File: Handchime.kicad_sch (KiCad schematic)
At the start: 24 parts, among them J1 USB_C_Receptacle_USB2.0_16P, J2 Pins, J3 SWD, SW0 BOOT, SW1 Row 0, Col 0, SW2 Row 0, Col 1, U1 STM32C071GBUx, U2 PRTR5V0U2X, U3 XC6206P332MR-G

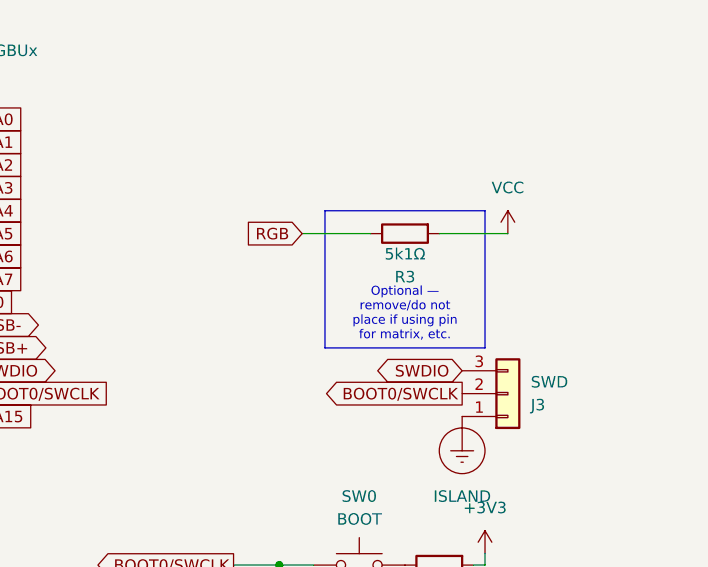
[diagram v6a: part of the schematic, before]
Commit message: Update labelling on optional RGB pull-op resistor
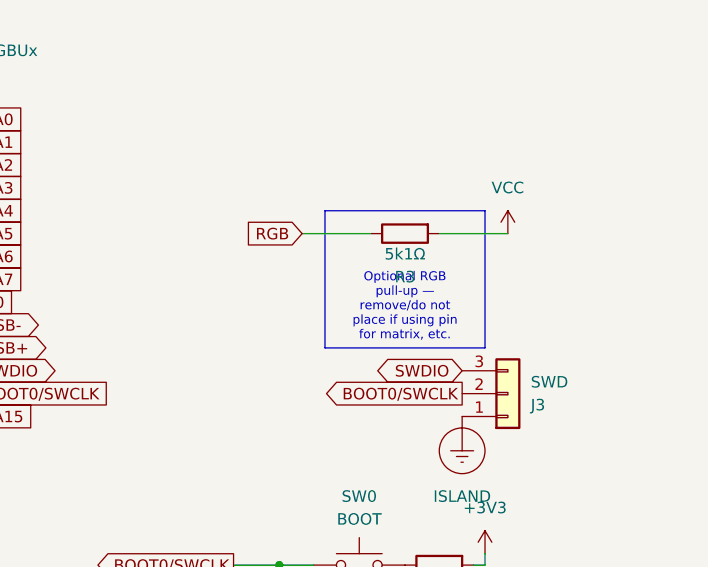
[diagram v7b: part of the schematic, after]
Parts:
- R3: Label (none) -> P
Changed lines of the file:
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@@
 		)
 	)
-	(text_box "Optional — remove/do not place if using pin for matrix, etc."
+	(text_box "Optional RGB pull-up — remove/do not place if using pin for matrix, etc."
 		(exclude_from_sim no)
 		(at 238.76 45.72 0)
@@
 			(at 247.65 48.26 90)
 			(hide yes)
+			(show_name no)
+			(do_not_autoplace no)
+			(effects
+				(font
+					(size 1.27 1.27)
+				)
+			)
+		)
+		(property "Label" "P"
+			(at 247.65 48.26 90)
+			(hide yes)

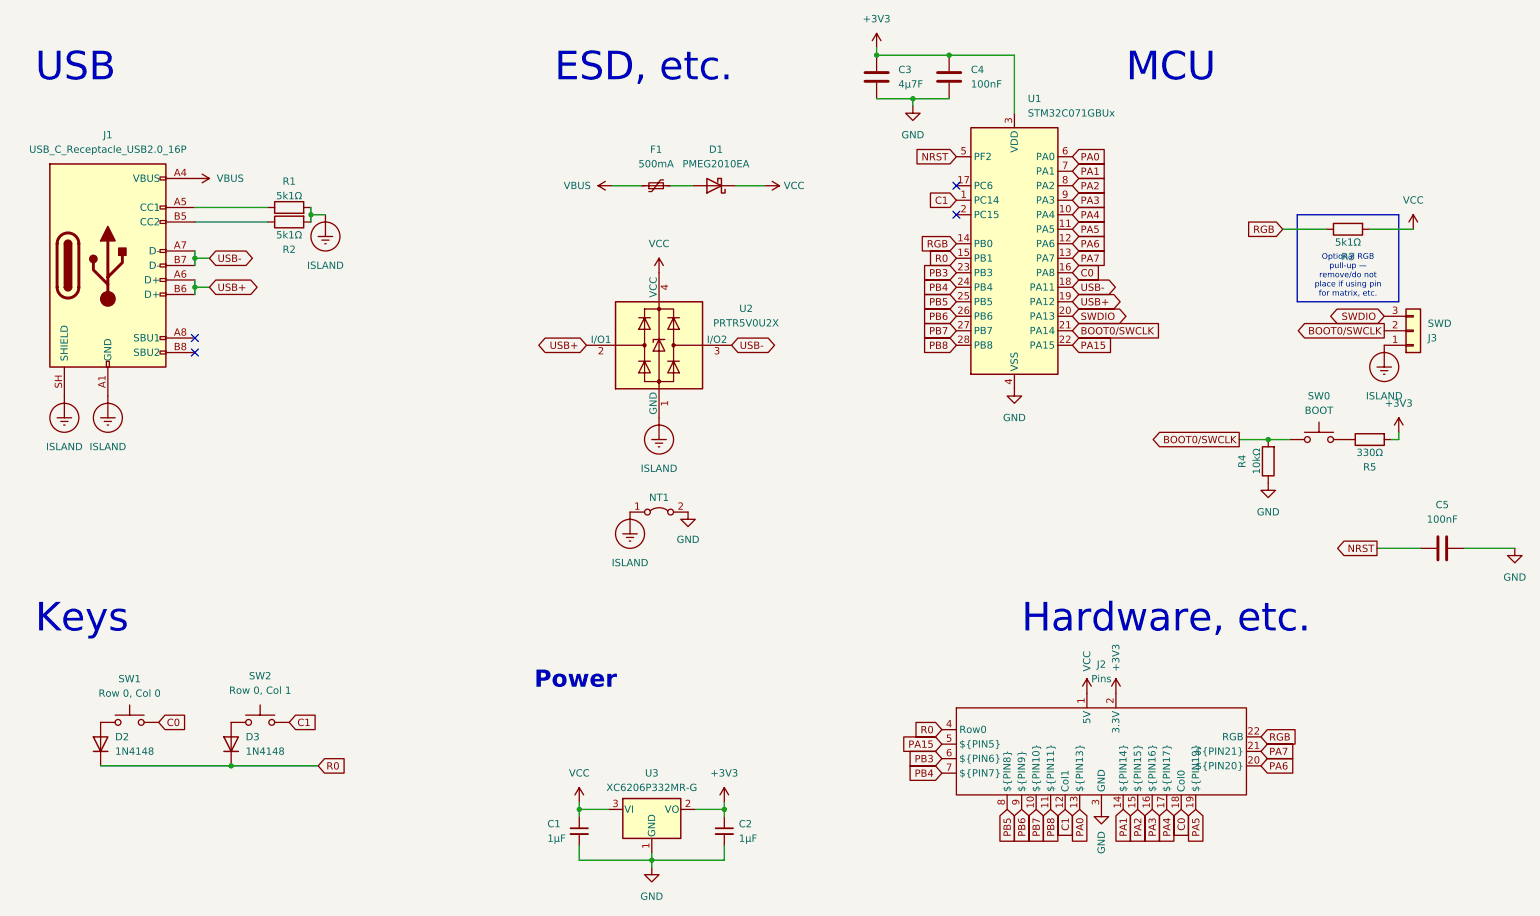
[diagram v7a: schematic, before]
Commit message: Add one extra GPIO pin access
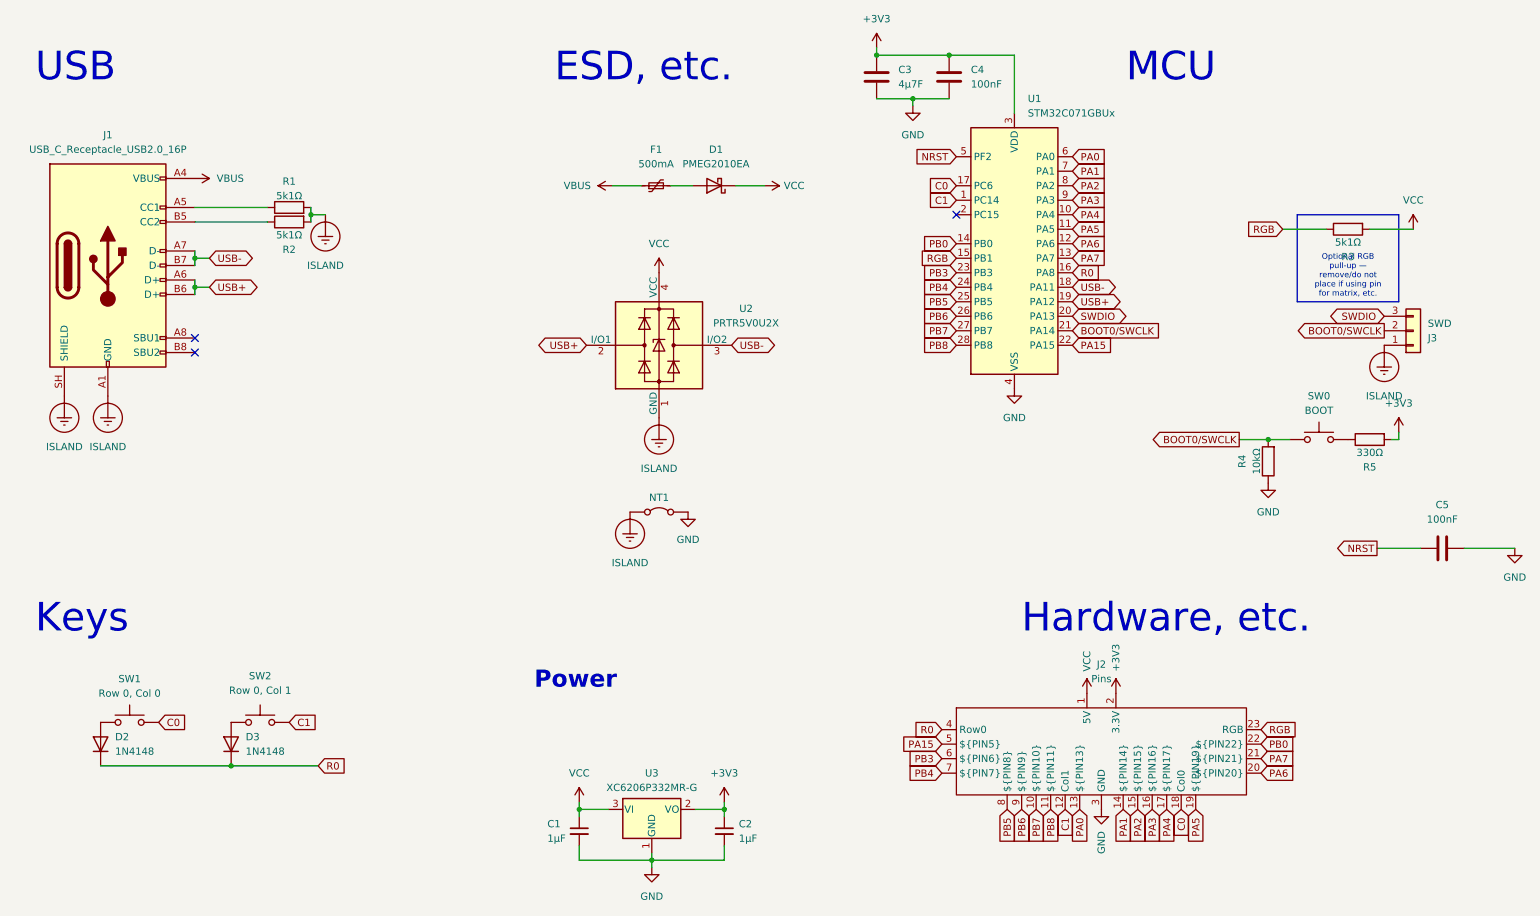
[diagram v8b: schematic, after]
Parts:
- J2: PIN22 (none) -> B0
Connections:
- net C0: now also U1.17 (PC6); no longer U1.16 (PA8)
- net R0: now also U1.16 (PA8); no longer U1.15 (PB1)
- net RGB: now also J2.23 (RGB), U1.15 (PB1); no longer J2.22 (RGB), U1.14 (PB0)
- new net PB0: J2.22 (${PIN22}), U1.14 (PB0)
- no-connect marks 4 -> 3
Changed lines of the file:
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@@
 	)
 	(no_connect
-		(at 179.07 40.64)
-	)
-	(no_connect
 		(at 45.72 67.31)
 	)
@@
 	(global_label "RGB"
 		(shape input)
-		(at 232.41 137.16 0)
+		(at 232.41 135.89 0)
 		(fields_autoplaced yes)
 		(effects
@@
 		)
 		(property "Intersheetrefs" "${INTERSHEET_REFS}"
-			(at 238.4645 137.16 0)
+			(at 238.4645 135.89 0)
 			(hide yes)
 			(show_name no)
@@
 		)
 	)
+	(global_label "PB0"
+		(shape input)
+		(at 232.41 138.43 0)
+		(fields_autoplaced yes)
+		(effects
+			(font
+				(size 1.27 1.27)
+			)
+			(justify left)
+		)
+		(property "Intersheetrefs" "${INTERSHEET_REFS}"
+			(at 238.3305 138.43 0)
+			(hide yes)
+			(show_name no)
+			(do_not_autoplace no)
+			(effects
+				(font
+					(size 1.27 1.27)
+				)
+				(justify left)
+			)
+		)
+	)
+	(global_label "C0"
+		(shape input)
+		(at 179.07 40.64 180)
+		(fields_autoplaced yes)
+		(effects
+			(font
+				(size 1.27 1.27)
+			)
+			(justify right)
+		)
+		(property "Intersheetrefs" "${INTERSHEET_REFS}"
+			(at 174.3146 40.64 0)
+			(hide yes)
+			(show_name no)
+			(do_not_autoplace no)
+			(effects
+				(font
+					(size 1.27 1.27)
+				)
+				(justify right)
+			)
+		)
+	)
 	(global_label "PA15"
 		(shape input)
@@
 	(global_label "PA6"
 		(shape input)
-		(at 232.41 142.24 0)
+		(at 232.41 143.51 0)
 		(fields_autoplaced yes)
 		(effects
@@
 		)
 		(property "Intersheetrefs" "${INTERSHEET_REFS}"
-			(at 238.0761 142.24 0)
+			(at 238.0761 143.51 0)
 			(hide yes)
 			(show_name no)
@@
 	(global_label "RGB"
 		(shape input)
-		(at 179.07 50.8 180)
+		(at 179.07 53.34 180)
 		(fields_autoplaced yes)
 		(effects
@@
 		)
 		(property "Intersheetrefs" "${INTERSHEET_REFS}"
-			(at 173.0155 50.8 0)
+			(at 173.0155 53.34 0)
 			(hide yes)
 			(show_name no)
@@
 	(global_label "PA7"
 		(shape input)
-		(at 232.41 139.7 0)
+		(at 232.41 140.97 0)
 		(fields_autoplaced yes)
 		(effects
@@
 		)
 		(property "Intersheetrefs" "${INTERSHEET_REFS}"
-			(at 237.9099 139.7 0)
+			(at 237.9099 140.97 0)
 			(hide yes)
 			(show_name no)
@@
 		)
 	)
-	(global_label "NRST"
-		(shape output)
-		(at 252.73 104.14 180)
+	(global_label "R0"
+		(shape input)
+		(at 199.39 55.88 0)
 		(fields_autoplaced yes)
 		(effects
@@
 				(size 1.27 1.27)
 			)
-			(justify right)
+			(justify left)
 		)
 		(property "Intersheetrefs" "${INTERSHEET_REFS}"
-			(at 245.7673 104.14 0)
+			(at 204.2571 55.88 0)
 			(hide yes)
 			(show_name no)
@@
 					(size 1.27 1.27)
 				)
-				(justify right)
+				(justify left)
 			)
 		)
 	)
-	(global_label "R0"
-		(shape input)
-		(at 179.07 53.34 180)
+	(global_label "NRST"
+		(shape output)
+		(at 252.73 104.14 180)
 		(fields_autoplaced yes)
 		(effects
@@
 		)
 		(property "Intersheetrefs" "${INTERSHEET_REFS}"
-			(at 174.2029 53.34 0)
+			(at 245.7673 104.14 0)
 			(hide yes)
 			(show_name no)
@@
 		)
 	)
-	(global_label "PB7"
+	(global_label "PB0"
 		(shape input)
-		(at 193.04 149.86 270)
+		(at 179.07 50.8 180)
 		(fields_autoplaced yes)
 		(effects
@@
 		)
 		(property "Intersheetrefs" "${INTERSHEET_REFS}"
-			(at 193.04 155.5733 90)
+			(at 173.1495 50.8 0)
 			(hide yes)
 			(show_name no)
@@
 		)
 	)
-	(global_label "C0"
+	(global_label "PB7"
 		(shape input)
-		(at 199.39 55.88 0)
+		(at 193.04 149.86 270)
 		(fields_autoplaced yes)
 		(effects
@@
 				(size 1.27 1.27)
 			)
-			(justify left)
+			(justify right)
 		)
 		(property "Intersheetrefs" "${INTERSHEET_REFS}"
-			(at 204.1454 55.88 0)
+			(at 193.04 155.5733 90)
 			(hide yes)
 			(show_name no)
@@
 					(size 1.27 1.27)
 				)
-				(justify left)
+				(justify right)
 			)
 		)
@@
 			)
 		)
-		(property "Description" ""
+		(property "Description" "Power symbol creates a global label with name \"VCC\""
 			(at 259.08 48.26 0)
 			(hide yes)
@@
 			)
 		)
-		(property "Description" ""
+		(property "Description" "Push button switch, generic, two pins"
 			(at 57.15 134.62 0)
 			(hide yes)
@@
 			)
 		)
-		(property "Description" ""
+		(property "Description" "Power symbol creates a global label with name \"GND\" , ground"
 			(at 233.68 92.71 0)
 			(hide yes)
@@
 			)
 		)
-		(property "Description" ""
+		(property "Description" "Resistor"
 			(at 62.23 44.45 0)
 			(hide yes)
@@
 			)
 		)
-		(property "Description" ""
+		(property "Description" "Power symbol creates a global label with name \"GND\" , ground"
 			(at 132.08 97.79 0)
 			(hide yes)
@@
 			)
 		)
-		(property "Description" ""
+		(property "Description" "Resistor"
 			(at 233.68 88.9 0)
 			(hide yes)
@@
 			)
 		)
-		(property "Description" ""
+		(property "Description" "Power symbol creates a global label with name \"VCC\""
 			(at 127 55.88 0)
 			(hide yes)
@@
 			)
 		)
-		(property "Description" ""
+		(property "Description" "Power symbol creates a global label with name \"VBUS\""
 			(at 45.72 39.37 0)
 			(hide yes)
@@
 			)
 		)
-		(property "Description" ""
+		(property "Description" "Power symbol creates a global label with name \"GND\" , ground"
 			(at 276.86 104.14 0)
 			(hide yes)
@@
 			)
 		)
-		(property "Description" ""
+		(property "Description" "Push button switch, generic, two pins"
 			(at 242.57 85.09 0)
 			(hide yes)
@@
 			)
 		)
-		(property "Description" ""
+		(property "Description" "Schottky diode"
 			(at 136.652 40.64 0)
 			(hide yes)
@@
 			)
 		)
-		(property "Description" ""
+		(property "Description" "Resettable fuse, polymeric positive temperature coefficient, small symbol"
 			(at 126.492 40.64 0)
 			(hide yes)
@@
 			)
 		)
-		(property "Description" ""
+		(property "Description" "Power symbol creates a global label with name \"GND\" , ground"
 			(at 171.45 26.67 0)
 			(hide yes)
@@
 			)
 		)
-		(property "Description" ""
+		(property "Description" "Power symbol creates a global label with name \"+3V3\""
 			(at 207.01 129.54 0)
 			(hide yes)
@@
 			)
 		)
-		(property "Description" ""
+		(property "Description" "Power symbol creates a global label with name \"VCC\""
 			(at 113.03 148.59 0)
 			(hide yes)
@@
 			)
 		)
-		(property "Description" ""
+		(property "Description" "Resistor"
 			(at 247.65 48.26 0)
 			(hide yes)
@@
 			)
 		)
-		(property "Description" ""
+		(property "Description" "Push button switch, generic, two pins"
 			(at 34.29 134.62 0)
 			(hide yes)
@@
 			)
 		)
-		(property "Description" ""
+		(property "Description" "Resistor"
 			(at 251.46 85.09 0)
 			(hide yes)
@@
 			)
 		)
-		(property "Description" ""
+		(property "Description" "Power symbol creates a global label with name \"VCC\""
 			(at 145.542 40.64 0)
 			(hide yes)
@@
 			)
 		)
-		(property "Description" ""
+		(property "Description" "Power symbol creates a global label with name \"VBUS\""
 			(at 118.872 40.64 0)
 			(hide yes)
@@
 			)
 		)
-		(property "Description" ""
+		(property "Description" "Power symbol creates a global label with name \"GND\" , ground"
 			(at 204.47 149.86 0)
 			(hide yes)
@@
 			)
 		)
-		(property "Description" ""
+		(property "Description" "Power symbol creates a global label with name \"GND\" , ground"
 			(at 189.23 76.2 0)
 			(hide yes)
@@
 			)
 		)
+		(property "PIN22" "B0"
+			(at 204.47 139.7 0)
+			(hide yes)
+			(show_name no)
+			(do_not_autoplace no)
+			(effects
+				(font
+					(size 1.27 1.27)
+				)
+			)
+		)
 		(pin "10"
 		)
@@
 		(pin "15"
 		)
+		(pin "23"
+		)
 		(instances
 			(project "Handchime"
@@
 			)
 		)
-		(property "Description" ""
+		(property "Description" "Jumper, 2-pole, closed/bridged"
 			(at 127 97.79 0)
 			(hide yes)
@@
 			)
 		)
-		(property "Description" ""
+		(property "Description" "Resistor"
 			(at 62.23 46.99 0)
 			(hide yes)
